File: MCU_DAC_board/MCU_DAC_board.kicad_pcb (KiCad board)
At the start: 4 copper layers, 100 x 100 mm, 102 parts, among them J1 Conn_02x04_Odd_Even, J11 105-0752-001, J12 Conn_01x03_Pin, J2 Conn_02x04_Odd_Even, J3 Conn_02x04_Odd_Even, J4 Conn_02x04_Odd_Even, J5 54-00127, J6 105-0752-001, J7 Screw_Terminal_01x02, J8 Screw_Terminal_01x02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

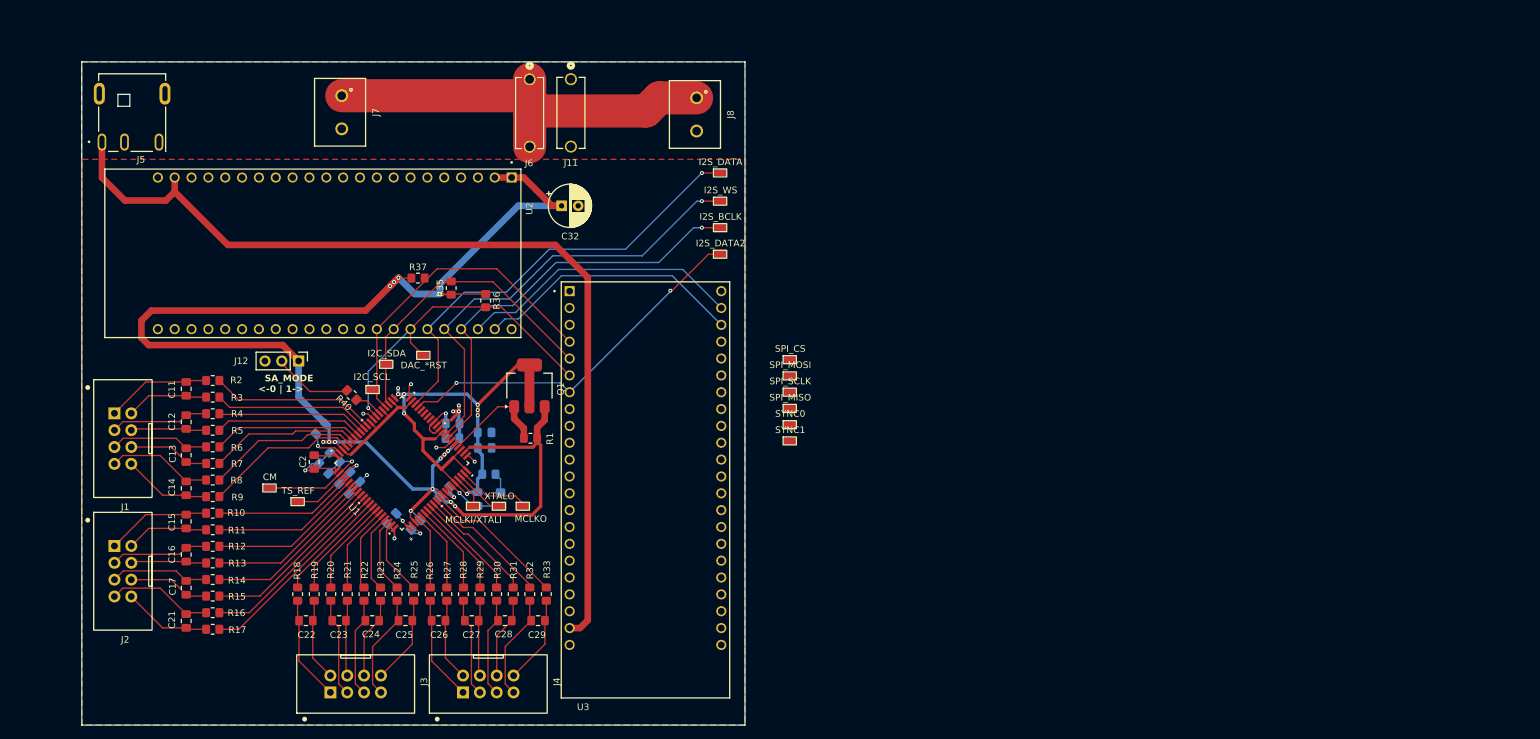
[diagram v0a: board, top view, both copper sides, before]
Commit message: Finished MCU to DAC signal routing
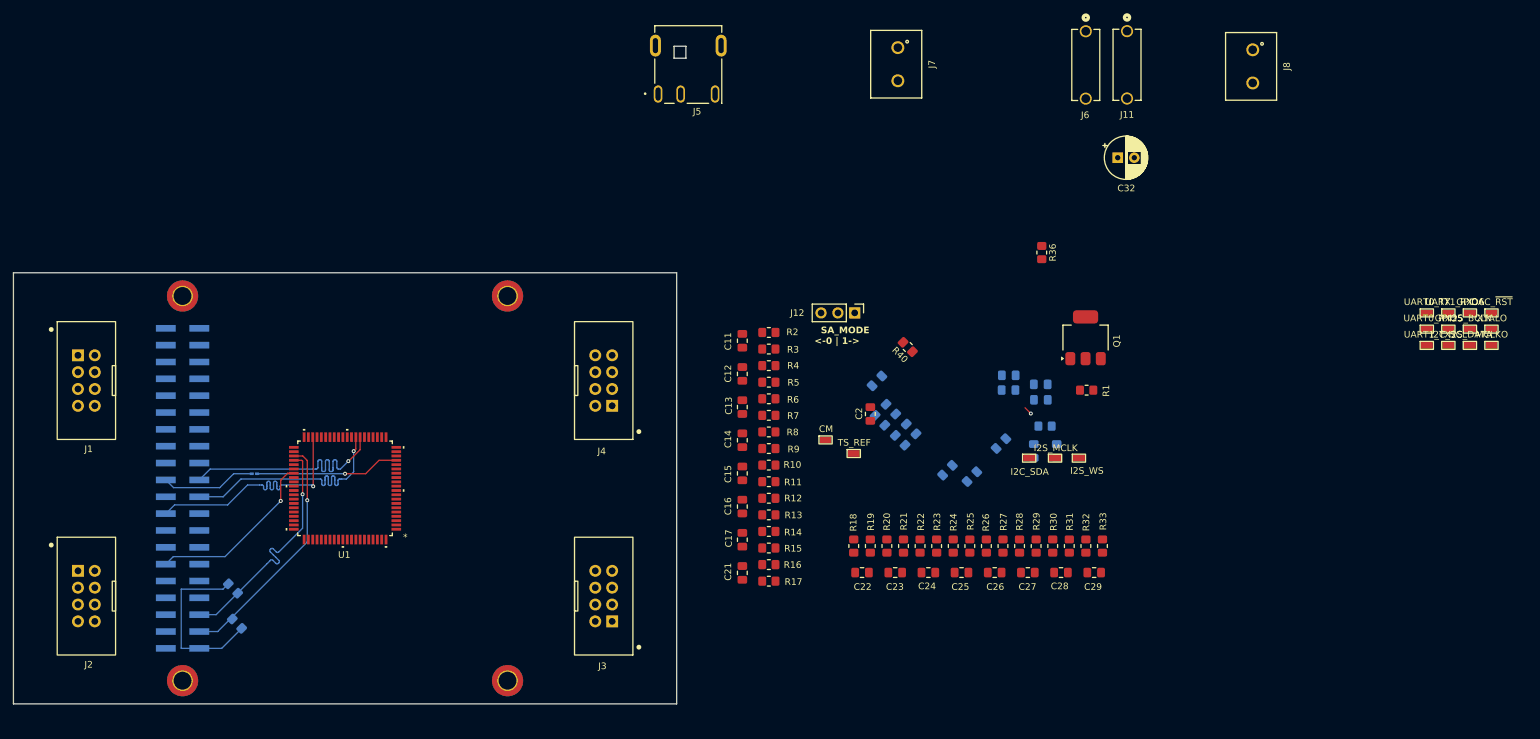
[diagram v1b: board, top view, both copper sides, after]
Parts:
- removed TP12: I2S_DATA2, project_lib:TP_1.8x1mm
- removed TP13: SPI_CS, project_lib:TP_1.8x1mm
- removed TP14: SPI_MOSI, project_lib:TP_1.8x1mm
- removed TP15: SPI_SCLK, project_lib:TP_1.8x1mm
- removed TP16: SPI_MISO, project_lib:TP_1.8x1mm
- removed TP17: SYNC0, project_lib:TP_1.8x1mm
- removed TP18: SYNC1, project_lib:TP_1.8x1mm
- removed TP4: I2S_BCLK, project_lib:TP_1.8x1mm
- removed TP5: I2S_WS, project_lib:TP_1.8x1mm
- removed TP6: DAC_*RST, project_lib:TP_1.8x1mm
- removed TP7: I2S_DATA, project_lib:TP_1.8x1mm
- removed TP8: I2C_SDA, project_lib:TP_1.8x1mm
- removed TP9: I2C_SCL, project_lib:TP_1.8x1mm
- removed U2, U3: ESP32-S3-DEVKITC-1-N8R2, project_lib:XCVR_ESP32-S3-DEVKITC-1-N8R2
- added H1: MountingHole_Pad, MountingHole:MountingHole_2.7mm_M2.5_DIN965_Pad_TopBottom, F.Cu at (157.3, 152.2)
- added H2: MountingHole_Pad, MountingHole:MountingHole_2.7mm_M2.5_DIN965_Pad_TopBottom, F.Cu at (108.3, 94.2)
- added H3: MountingHole_Pad, MountingHole:MountingHole_2.7mm_M2.5_DIN965_Pad_TopBottom, F.Cu at (108.3, 152.2)
- added H4: MountingHole_Pad, MountingHole:MountingHole_2.7mm_M2.5_DIN965_Pad_TopBottom, F.Cu at (157.3, 94.2)
- added J9: Conn_02x20_Odd_Even, Connector_PinSocket_2.54mm:PinSocket_2x20_P2.54mm_Vertical_SMD, B.Cu at (108.3, 123.2)
- added JP1: SolderJumper_2_Open, Resistor_SMD:R_0201_0603Metric_Pad0.64x0.40mm_HandSolder, B.Cu at (119.1, 121.0)
- added TP19: UART0_TX, project_lib:TP_1.8x1mm, F.Cu at (295.9, 96.7)
- added TP20: UART0_RX, project_lib:TP_1.8x1mm, F.Cu at (295.9, 99.2)
- added TP21: UART1_TX, project_lib:TP_1.8x1mm, F.Cu at (295.9, 101.6)
- added TP22: UART1_RX, project_lib:TP_1.8x1mm, F.Cu at (299.1, 96.7)
- added TP23: GPIO5, project_lib:TP_1.8x1mm, F.Cu at (299.1, 99.2)
- added TP24: I2C_SCL, project_lib:TP_1.8x1mm, F.Cu at (299.1, 101.6)
- added TP25: GPIO6, project_lib:TP_1.8x1mm, F.Cu at (302.4, 96.7)
- added TP26: I2S_BCLK, project_lib:TP_1.8x1mm, F.Cu at (302.4, 99.2)
- added TP27: I2S_DATA, project_lib:TP_1.8x1mm, F.Cu at (302.4, 101.6)
- added TP28: DAC_~{RST}, project_lib:TP_1.8x1mm, F.Cu at (305.6, 96.7)
- added TP29: XTALO, project_lib:TP_1.8x1mm, F.Cu at (305.6, 99.2)
- added TP30: MCLKO, project_lib:TP_1.8x1mm, F.Cu at (305.6, 101.6)
- R35, R37: moved to B.Cu
- TP1: value MCLKI/XTALI -> I2C_SDA
- TP2: value XTALO -> I2S_MCLK
- TP3: value MCLKO -> I2S_WS
- moved J6 84.2 mm to (244.5, 54.2)
- moved C11 84.2 mm to (192.7, 100.9)
- moved C12 84.2 mm to (192.7, 105.9)
- moved C13 84.2 mm to (192.7, 110.9)
- moved C14 84.2 mm to (192.7, 115.9)
- moved C15 84.2 mm to (192.7, 120.9)
- moved C16 84.2 mm to (192.7, 125.9)
- moved C17 84.2 mm to (192.7, 130.9)
- moved C21 84.2 mm to (192.7, 135.9)
- moved R10 84.2 mm to (196.7, 119.7)
- moved R11 84.2 mm to (196.7, 122.2)
- moved R12 84.2 mm to (196.7, 124.7)
- moved R13 84.2 mm to (196.7, 127.2)
- moved R14 84.2 mm to (196.7, 129.7)
- moved R15 84.2 mm to (196.7, 132.2)
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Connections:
- net /DAC_*RST renamed /DAC_~{RST}
- R35 pad 1: +3V3 -> +3V3_MCU
- R35 pad 2: /I2C_SDA -> /GPIO8
- R37 pad 1: +3V3 -> +3V3_MCU
- R37 pad 2: /I2C_SCL -> /GPIO7
- TP1 pad 1: /MCLKI/XTALI -> /GPIO7
- TP2 pad 1: /XTALO -> /GPIO1
- TP3 pad 1: /MCLKO -> /GPIO3
- U1 pad 17: /MCLKI/XTALI -> /GPIO1
- U1 pad 18: /XTALO -> Net-(U1-XTALO)
- U1 pad 19: /MCLKO -> Net-(U1-MCLKO)
- U1 pad 27: /I2S_BCLK -> /GPIO2
- U1 pad 28: /I2S_WS -> /GPIO3
- U1 pad 37: /I2S_DATA2 -> unconnected-(U1-DSDATA2-Pad37)
- U1 pad 38: /I2S_DATA1 -> /GPIO4
- U1 pad 43: /I2C_SDA -> /GPIO7
- U1 pad 44: /I2C_SCL -> /GPIO8
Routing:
- net +3V3: track 266.0 -> 0.00 mm, vias 17 -> 0
- net +5V: track 143.0 -> 0.00 mm
- net +2V5: track 79.4 -> 0.00 mm, vias 8 -> 0
- net /I2S_WS: track 67.9 -> 0.00 mm, vias 1 -> 0
- net /I2S_DATA1: track 67.3 -> 0.00 mm, vias 1 -> 0
- net +24V: track 65.4 -> 0.00 mm
- net /I2S_BCLK: track 63.8 -> 0.00 mm, vias 1 -> 0
- net /I2S_DATA2: track 56.3 -> 0.00 mm, vias 2 -> 0
- net /I2C_SCL: track 49.7 -> 0.00 mm
- net /I2C_SDA: track 46.3 -> 0.00 mm
- net /USART_RX: track 42.8 -> 0.00 mm
- net /USART_TX: track 40.5 -> 0.00 mm
- net GND: track 39.9 -> 1.30 mm, vias 9 -> 1
- net /GPIO3: track 0.00 -> 37.9 mm, vias 0 -> 1
- net /GPIO4: track 0.00 -> 36.8 mm, vias 0 -> 1
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- removed copper zone on B.Cu, net GND
- removed copper zone on F.Cu, net GND
- removed copper zone on In2.Cu, net GND
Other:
- board size 100 x 100 mm -> 100 x 65 mm

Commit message: DAC board layout (mostly) done
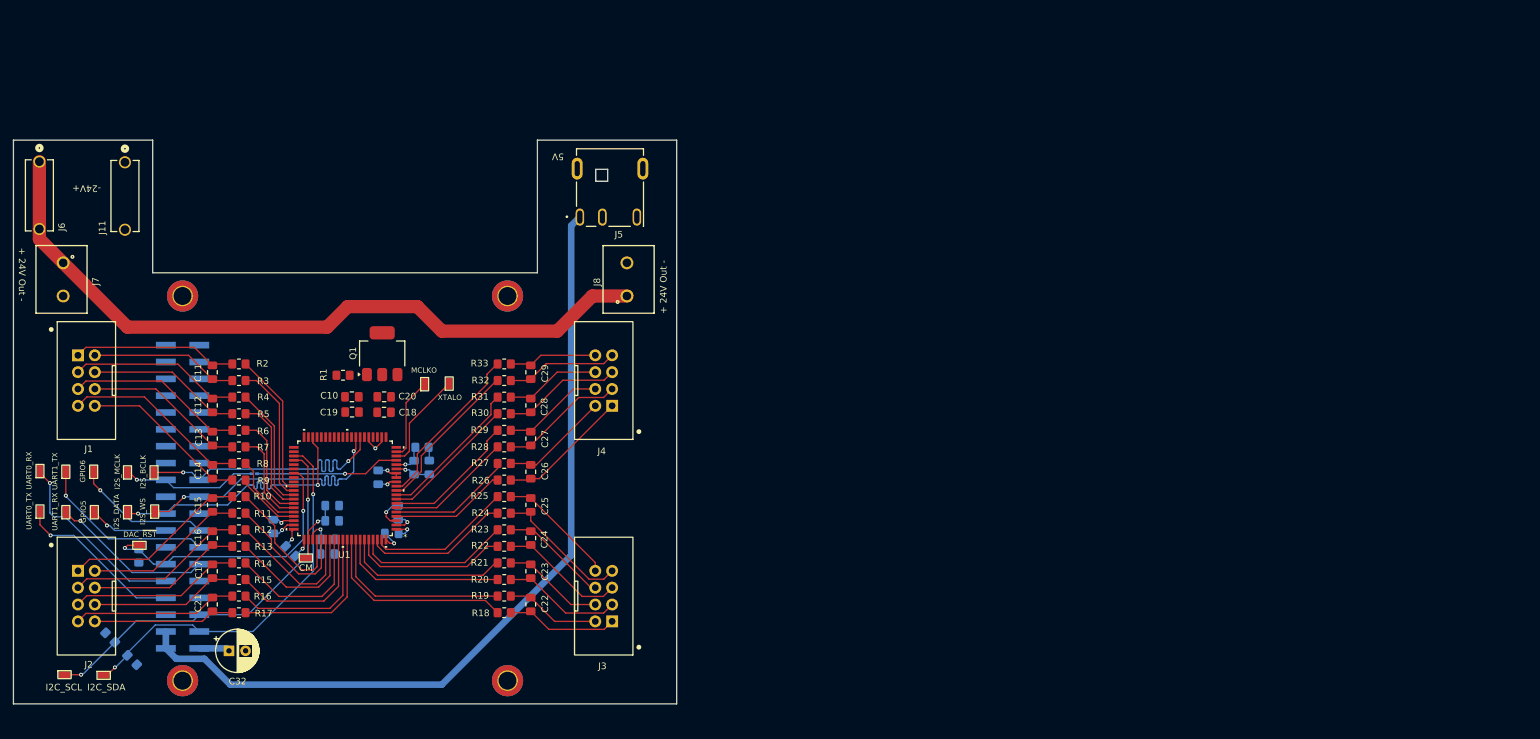
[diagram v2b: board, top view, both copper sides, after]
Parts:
- removed J12: Conn_01x03_Pin, Connector_PinHeader_2.54mm:PinHeader_1x03_P2.54mm_Vertical
- removed R40: 2k, Resistor_SMD:R_0805_2012Metric_Pad1.20x1.40mm_HandSolder
- removed TP10: TS_REF, project_lib:TP_1.8x1mm
- C10, C18, C19, C20: moved to F.Cu
- C2, R36: moved to B.Cu
- moved TP24 214.5 mm to (90.5, 151.3)
- moved TP19 211.2 mm to (86.8, 126.7), turned to 90 degrees
- moved TP22 210.6 mm to (90.7, 126.8), turned to 90 degrees
- moved TP20 210.2 mm to (86.8, 120.6), turned to 90 degrees
- moved TP25 208.9 mm to (94.9, 120.7), turned to 90 degrees
- moved TP28 206.8 mm to (101.8, 131.8)
- moved TP21 206.1 mm to (90.7, 120.7), turned to 90 degrees
- moved TP23 206.0 mm to (95.0, 126.8), turned to 90 degrees
- moved TP27 204.0 mm to (100.0, 126.8), turned to 90 degrees
- moved TP26 199.6 mm to (104.0, 120.8), turned to 90 degrees
- moved TP30 161.0 mm to (144.8, 107.5), turned to 90 degrees
- moved J6 159.0 mm to (86.7, 73.9)
- moved TP29 157.4 mm to (148.5, 107.4), turned to 90 degrees
- moved C32 153.2 mm to (115.3, 147.7)
- moved J11 152.4 mm to (99.6, 74.0)
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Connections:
- J9 pad 1: +3V3_MCU -> +3V3
- J9 pad 17: +3V3_MCU -> +3V3
- JP1 pad 2: /GPIO1 -> Net-(JP1-B)
- R35 pad 1: +3V3_MCU -> +3V3
- R37 pad 1: +3V3_MCU -> +3V3
- U1 pad 17: /GPIO1 -> Net-(JP1-B)
- U1 pad 46: /SA_MODE -> unconnected-(U1-SA_MODE-Pad46)
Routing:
- net +5V: track 0.00 -> 125.5 mm
- net +24V: track 0.00 -> 110.8 mm
- net /DAC9P: track 0.00 -> 30.0 mm
- net /GPIO38: track 0.00 -> 28.7 mm, vias 0 -> 1
- net /DAC9N: track 0.00 -> 28.2 mm
- net /DAC_filter/Out4P: track 0.00 -> 28.2 mm
- net /DAC_filter1/Out1P: track 0.00 -> 27.9 mm
- net /DAC_filter/Out3P: track 0.00 -> 27.0 mm
- net /GPIO20: track 0.00 -> 27.0 mm, vias 0 -> 1
- net /DAC_filter1/Out2P: track 0.00 -> 26.9 mm
- net +3V3_MCU: track 26.7 -> 0.00 mm
- net /DAC_filter/Out2P: track 0.00 -> 26.0 mm
- net /DAC_filter1/Out3P: track 0.00 -> 25.9 mm
- net /GPIO37: track 0.00 -> 25.5 mm, vias 0 -> 1
- net /DAC_filter/Out4N: track 0.00 -> 25.4 mm
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- removed copper zone on In1.Cu, net GND
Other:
- board size 100 x 65 mm -> 100 x 85 mm
- board text added: "+ 24V Out -"
- board text added: "-24V+"
- board text added: "5V"
- board text added: "Tall USB Ports on the P4 go Here :P"
- board text removed: "SA_MODE <-0 | 1->"

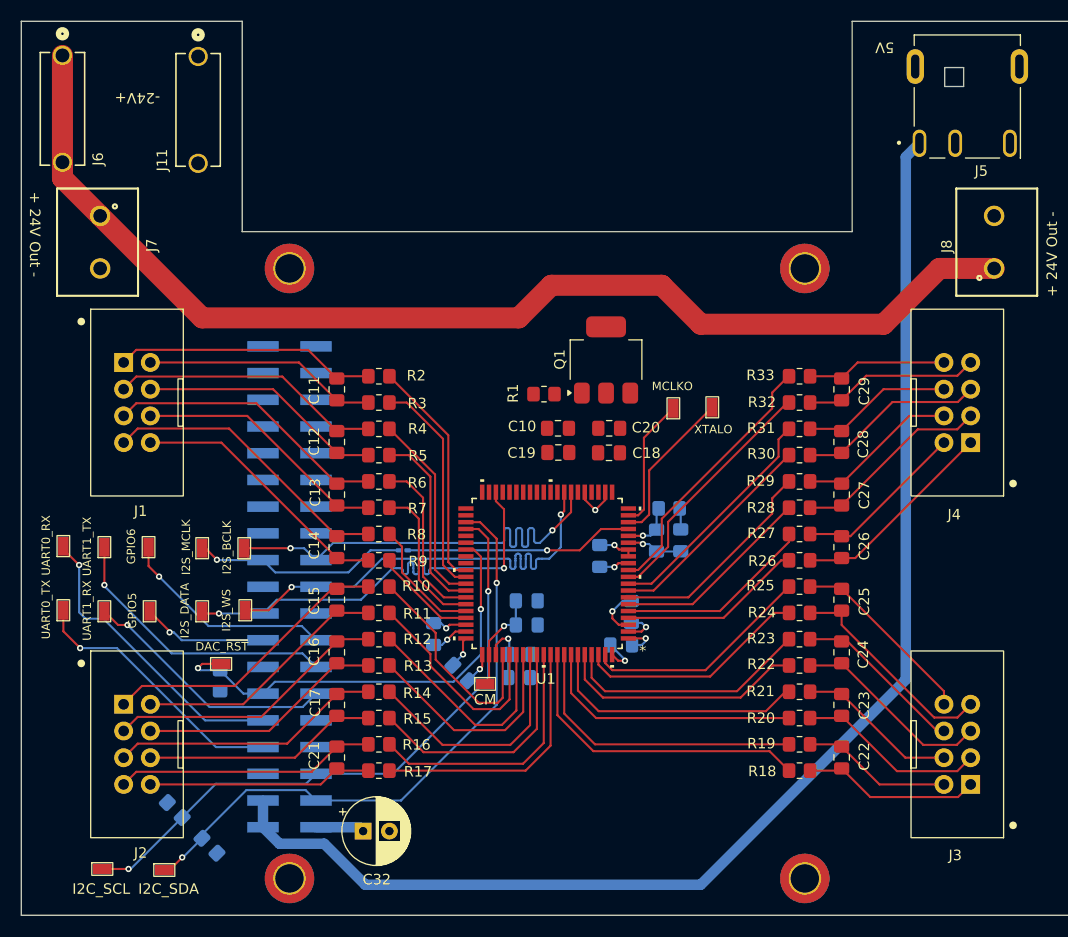
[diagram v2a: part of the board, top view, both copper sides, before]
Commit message: Added DIP conector for UART connections
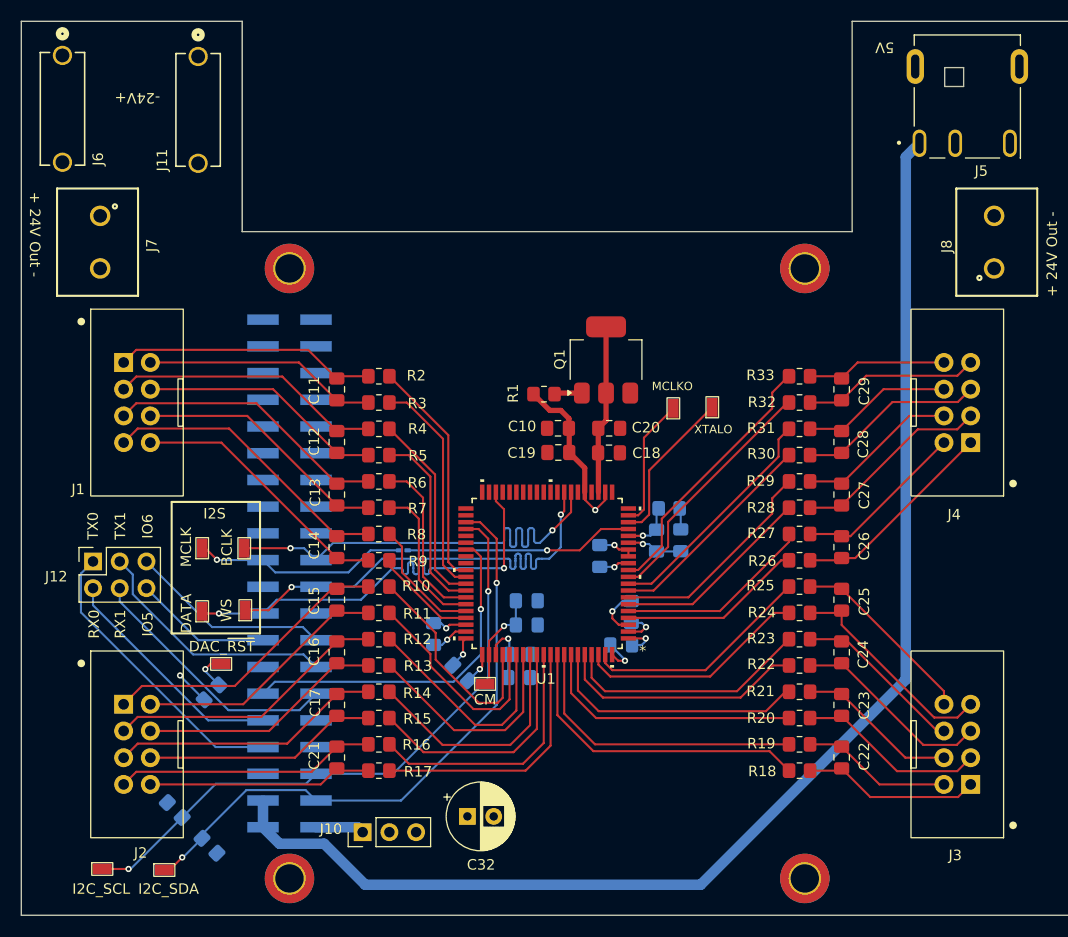
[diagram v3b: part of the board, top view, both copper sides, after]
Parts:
- removed TP19: UART0_TX, project_lib:TP_1.8x1mm
- removed TP20: UART0_RX, project_lib:TP_1.8x1mm
- removed TP21: UART1_TX, project_lib:TP_1.8x1mm
- removed TP22: UART1_RX, project_lib:TP_1.8x1mm
- removed TP23: GPIO5, project_lib:TP_1.8x1mm
- removed TP25: GPIO6, project_lib:TP_1.8x1mm
- added J10: Conn_01x03_Pin, Connector_PinHeader_2.54mm:PinHeader_1x03_P2.54mm_Vertical, F.Cu at (115.2, 147.8)
- added J12: Conn_02x03_Odd_Even, Connector_PinSocket_2.54mm:PinSocket_2x03_P2.54mm_Vertical, F.Cu at (89.6, 122.0)
- TP2: value I2S_MCLK -> MCLK
- TP26: value I2S_BCLK -> BCLK
- TP27: value I2S_DATA -> DATA
- TP3: value I2S_WS -> WS
- moved C32 10.0 mm to (125.2, 146.3)
- moved R36 1.37 mm to (100.9, 134.5), turned to 45 degrees
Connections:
- J9 pad 1: +3V3 -> +3V3_MCU
- J9 pad 17: +3V3 -> unconnected-(J9-Pin_17-Pad17)
- R35 pad 1: +3V3 -> +3V3_MCU
- R37 pad 1: +3V3 -> +3V3_MCU
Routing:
- net +24V: track 110.8 -> 0.00 mm
- net +2V5: track 5.03 -> 21.1 mm
- net +3V3: track 19.9 -> 30.5 mm, vias 4 -> 5
- net /GPIO38: track 28.7 -> 22.3 mm, vias 1 -> 0
- net /DAC_~{RST}: track 42.8 -> 37.0 mm
- net +3V3_MCU: track 0.00 -> 4.63 mm
- net /GPIO20: track 27.0 -> 23.9 mm, vias 1 -> 0
- net /VDRIVE: track 0.00 -> 2.64 mm
- net /GPIO37: track 25.5 -> 27.9 mm, vias 1 -> 0
- net /GPIO6: track 20.6 -> 19.2 mm, vias 1 -> 0
- net /GPIO5: track 12.0 -> 13.1 mm, vias 1 -> 0
- net /GPIO21: track 24.4 -> 24.9 mm, vias 1 -> 0
- added copper zone on In1.Cu, net +24V
- added copper zone on In1.Cu, net +3V3
- added copper zone on In2.Cu, net GND
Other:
- board text added: "I2S"
- board text added: "IO5"
- board text added: "IO6"
- board text added: "RX0"
- board text added: "RX1"
- board text added: "TX0"
- board text added: "TX1"
